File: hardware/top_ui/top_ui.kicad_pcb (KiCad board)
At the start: 4 copper layers, 47 x 47 mm, 25 parts, among them J2 J_STK_A, J3 J_STK_B, J5 ER-TFT1.69-3, J6 Stern (intern), Q1 BC847, Q2 P-FET 20V 1A, SW1 BTN1, SW2 BTN2, SW3 BTN3, SW4 BTN4, U2 SHT40-AD1B, U3 VL53L1X

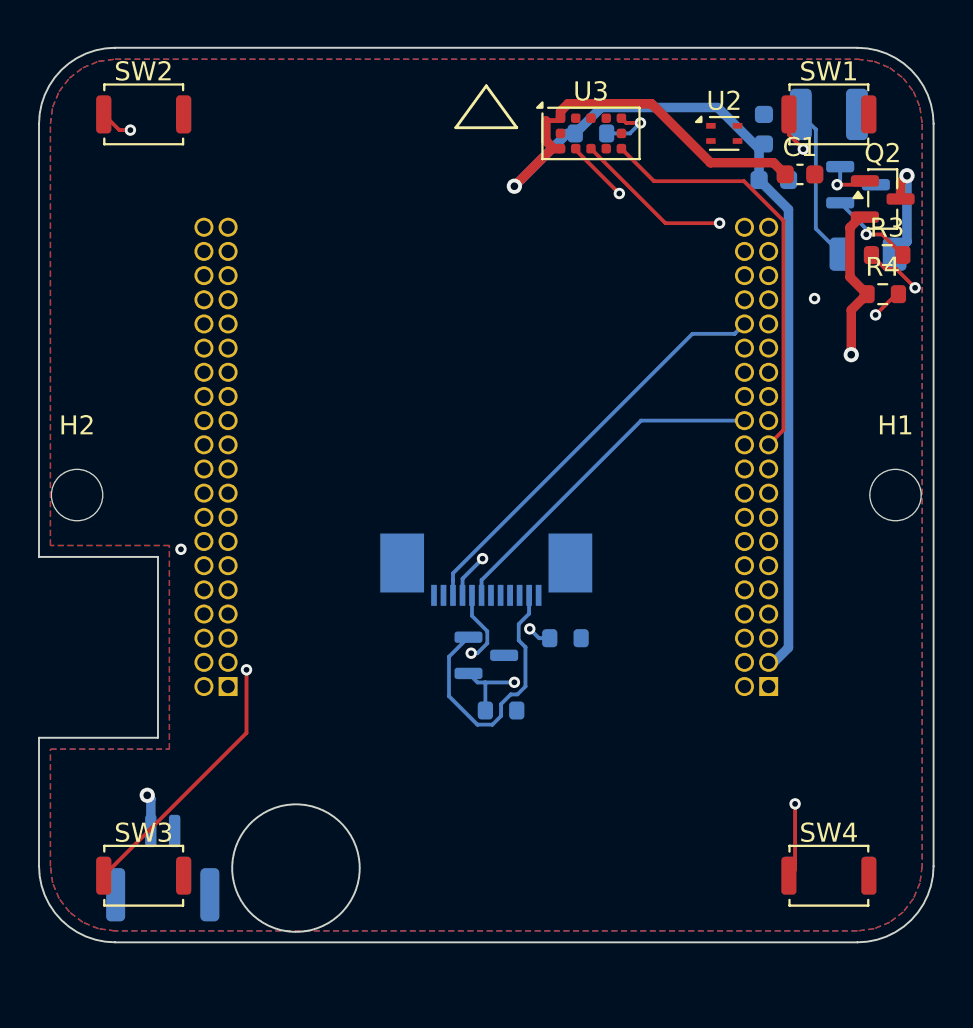
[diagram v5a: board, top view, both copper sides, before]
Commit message: Hauptschalter, Magnetkontakt im Rahmen, verschraubter Stapel - Umbau v0.7
VIER ENTSCHEIDUNGEN VOM 19.08.2026, alle umgesetzt:

1. HAUPTSCHALTER. Bisher stand nach dem Verschrauben von Bottom und Mid
sofort 24 V auf allem - ohne dass das Top-Board steckte. Jetzt laeuft der
Gate-Pulldown des Verpolschutz-FETs als SCHLEIFE durch den Stapel:
Q1-Gate -> R1 -> EN_LOOP (Stapelkontakt B2, war PGND; Pinout v0.7) -> SW5
auf Top -> PGND. Neuer 1-M-Pullup R1B haelt das Gate bei offener Schleife
definiert an der Source. Top-Board fehlt ODER SW5 aus -> Q1 sperrt, nichts
bekommt 24 V. Der Schalter traegt nur den Teilerstrom (~20 uA).
SW5 ist ein Copal CVS-01 (1,5 mm hoch, unter der Scheibe, durch eine
Oeffnung bedienbar). Er sitzt HOCHKANT bei (11,9/-19,4): Das Fenster
zwischen ToF-Courtyard (bis 8,245) und Ecktaster (ab 15,205) ist 6,96 mm
breit, der Schalter waagerecht 7,69 - drei Anlaeufe bei 12,5, 11,0 und 11,9
endeten in DRC-Ueberlappungen, erst das Ausmessen statt Schaetzens der
Courtyards zeigte, dass NUR gedreht Platz ist.

2. MAGNETKONTAKT IN DEN ABDECKRAHMEN, unten mittig - dort haelt auch das
vorhandene DCX-909 (Gewinde OD 8, im Rahmen ist Platz; Messpunkt F14: ist
der Rahmen dort hohl?). Das Magnetlangloch im Top-Board (Zwischenloesung
von einem Tag) ist wieder raus, mit ihm die 6,8-mm-Grenze, an der jedes
Kaufteil scheiterte. Neu: KABELKERBE 5 x 2 unten mittig, J6 dahinter
mittig auf der Rueckseite. Router-Keepout entsprechend getauscht.

3. LOETSCHEIBE hardware/stern_puck/ (OE 16, zweilagig, DRC null Fehler):
verbindet die Steckseite des DCX-909 mit den Litzen des Sterns. Litzen
durch Fesselbohrungen faedeln, umschlagen, loeten - die Zugentlastung ist
die Bohrung, nicht das Zinn. Drei eigene DRC-Runden gebraucht: 2,0er Pads
beruehren sich bei 1,85 Stiftabstand, die Minus-Bruecke lief durch das
Plus-Pad, die Fesselbohrungen brauchten seitliche Lage und OE 16 statt 14.

4. BEFESTIGUNGSKONZEPT v2 (docs/04, 2b): verschraubt statt nur gesteckt.
NEU mechanical/tragring.py 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
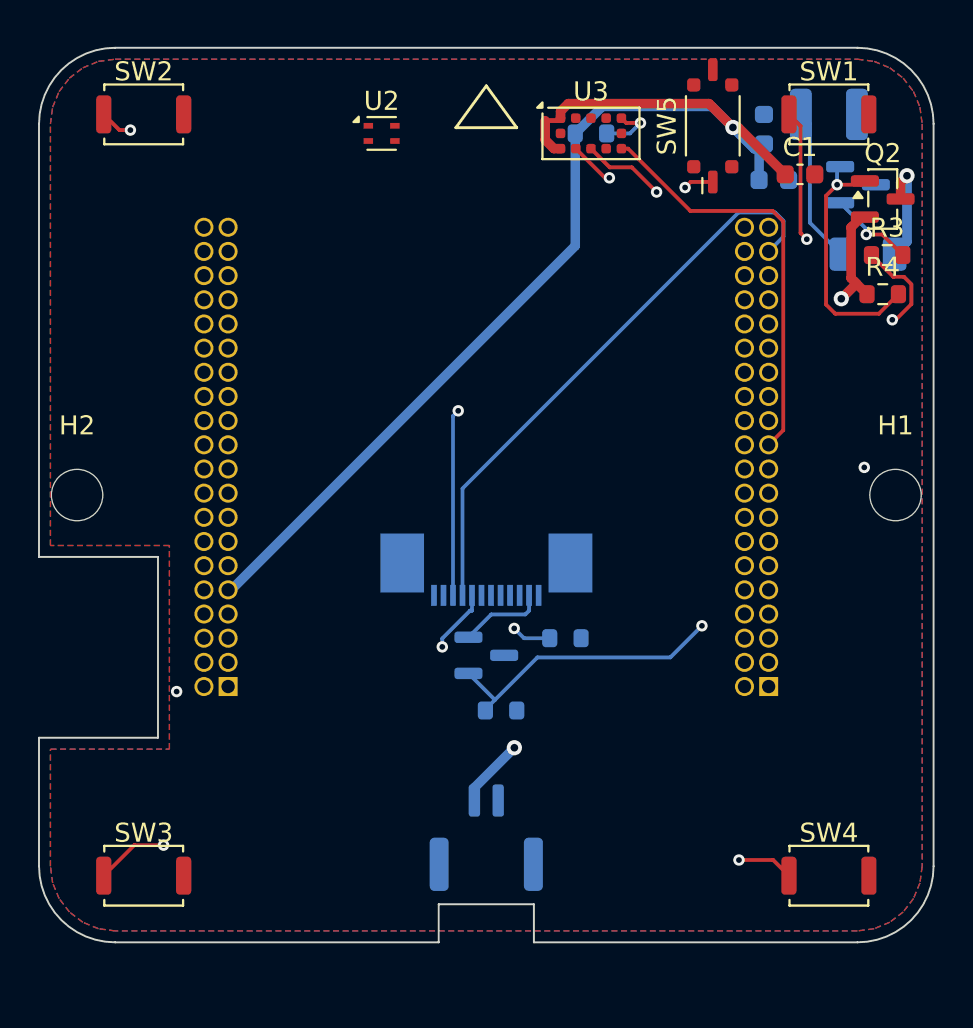
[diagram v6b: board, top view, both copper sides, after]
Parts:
- added SW5: HAUPT, SW_DIP_SPSTx01_Slide_Copal_CVS-01xB_W5.9mm_P1mm, F.Cu at (11.9, -19.4)
- moved U2 18.0 mm to (-5.50, -19.0)
- moved J6 17.1 mm to (0.00, 18.0)
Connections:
- J3 pad 2: PGND -> EN_LOOP
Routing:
- net EN_LOOP: track 0.00 -> 29.1 mm, vias 0 -> 1
- net QSPI_CLK: track 18.1 -> 0.00 mm
- net STAR_OUT: track 67.7 -> 55.0 mm
- net DISP_LEDK: track 14.5 -> 4.57 mm
- net BTN4: track 35.6 -> 41.0 mm
- net QSPI_D1: track 21.9 -> 26.7 mm, vias 0 -> 1
- net DISP_BL: track 31.7 -> 35.8 mm
- net BTN3: track 40.2 -> 37.2 mm
- net 6V2_STAR_F: track 53.9 -> 51.3 mm
- net 3V3_SYS: track 94.8 -> 92.8 mm
- net STAR_G: track 11.9 -> 13.5 mm, vias 2 -> 1
- net BTN2: track 32.6 -> 33.8 mm
- net QSPI_D0: track 41.5 -> 42.7 mm
- net STAR_EN: track 46.0 -> 47.2 mm
- net I2C_SDA: track 34.0 -> 33.3 mm
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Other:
- outline, holes or cut-outs redrawn
